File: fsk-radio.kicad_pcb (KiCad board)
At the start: 4 copper layers, 48.8 x 20 mm, 66 parts, among them IC1 STM32F4xx-QFN48, IC2 AT86RF215, IC3 LM3671, IC4 NC7SZ04, IC6 W25Q32BVZPIP, IC7 DPX202700DT, J1 USB_A, J2 Conn_01x06, J3 CONN_02X05, J4 RF_Shield_One_Piece, J5 RF_Shield_One_Piece, J6 Conn_01x06, J7 SMA, J8 Conn_01x06, SW1 SW_Push, X1 TXETBLSANF-26

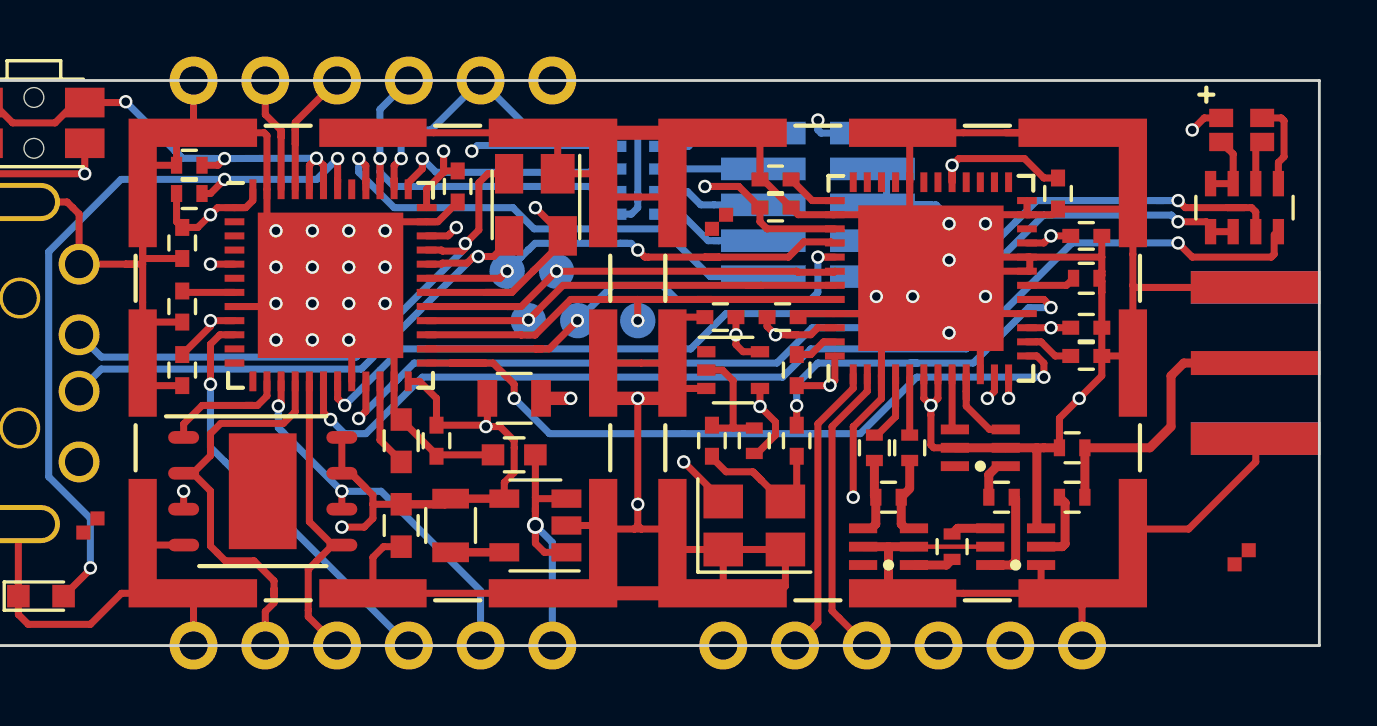
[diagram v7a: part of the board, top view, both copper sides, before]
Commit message: Final update to PCB for manufacturing release.
Capacitor C22 moved to improve clearance with the RF shield and switch
to using checker-mark pattern for fiducials. Other minor adjustments to
the fab reference, silkscreen and paste layers.
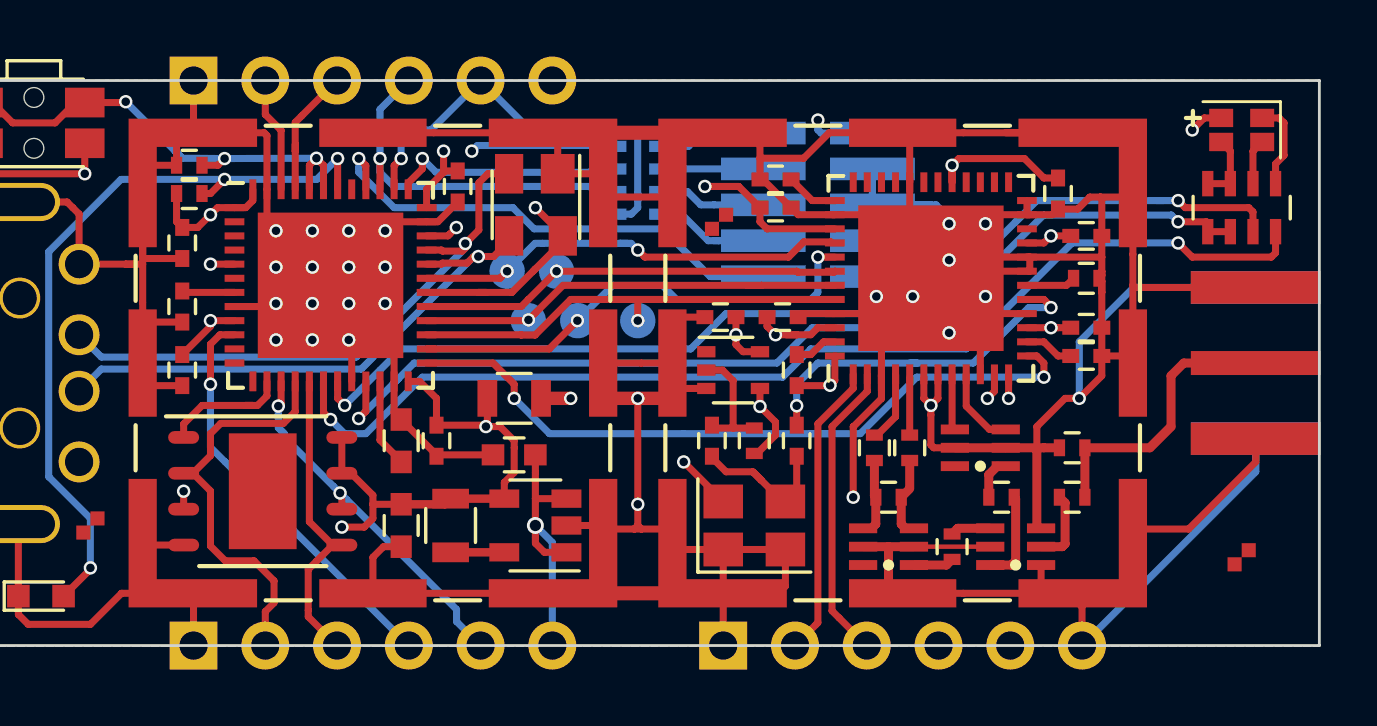
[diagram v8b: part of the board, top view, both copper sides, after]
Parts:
- C17, C4: value C -> 100n
- C29: value C -> 15pF
- J4, J5: footprint Shielding_Cabinets:Laird_Technologies_BMI-S-102_16.50x16.50mm -> FSK Parts:Laird_Technologies_BMI-S-102_16.50x16.50mm_Paste
- R3: value R3 -> R
- moved RN1 0.10 mm to (194.5, 94.5)
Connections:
- J8 pad 1: Net-(J8-Pad1) -> GND
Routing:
- net GND: track 340.5 -> 368.8 mm
- net /CPU/~RF_NRST: track 27.2 -> 26.0 mm
- net /CPU/SPI_MISO: track 16.9 -> 15.7 mm
- net VCC: track 129.2 -> 128.2 mm
- net /CPU/RF_IRQ: track 16.6 -> 15.6 mm
- net /RF/RF09-: track 4.39 -> 3.52 mm
- net /CPU/FL_SCLK: track 14.1 -> 13.2 mm
- net /CPU/GREEN: track 38.3 -> 37.6 mm
- net /CPU/~SPI_CS: track 15.7 -> 15.0 mm
- net +5V: track 47.3 -> 46.6 mm
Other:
- board text removed: "~CS"
